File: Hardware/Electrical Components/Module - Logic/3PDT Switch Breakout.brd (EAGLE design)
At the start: 15.2 x 21.3 mm, 2 parts

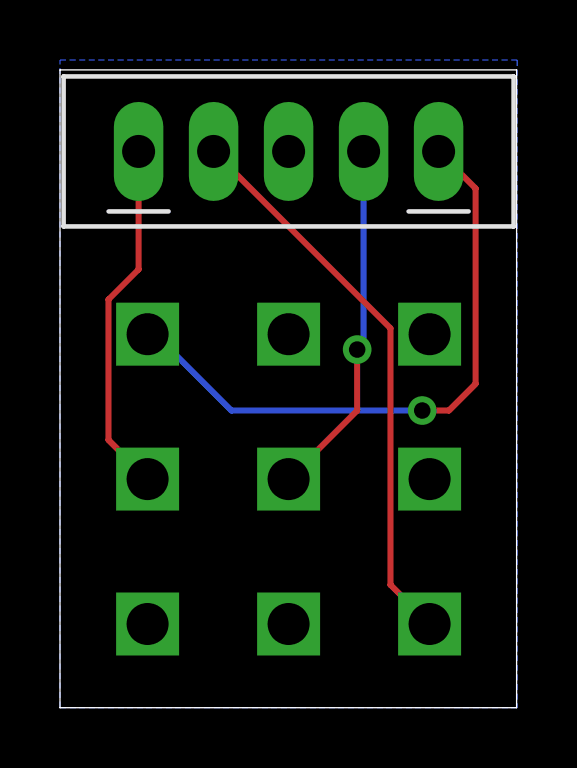
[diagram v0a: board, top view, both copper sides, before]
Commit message: Clarify text in PCBs
O Add text for 3PDT Switch breakout board better PCB annotation
O Rename MOSFET that controls LED for Programming Mode -> P_MOS
+ Add JST Male to BOM Logic Module – Power V8
O Correct excel formula for a total price of Logic Module
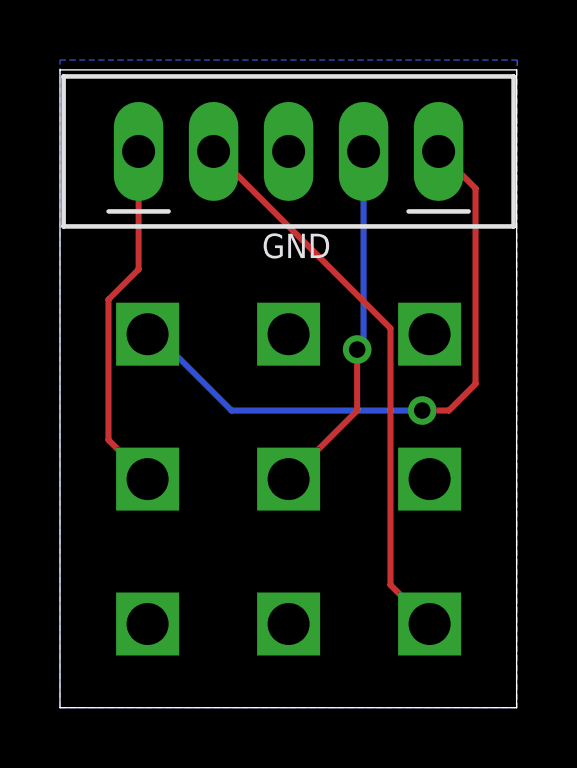
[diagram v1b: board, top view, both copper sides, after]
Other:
- board text added: "Latch"
- board text added: "SD"
- board text added: "Wake_NoSleep"
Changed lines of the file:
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@@
 <wire x1="0" y1="21.26" x2="0" y2="0" width="0" layer="20"/>
 <text x="0.508" y="9.398" size="1" layer="51" rot="R270">ON ON</text>
-<text x="11.938" y="15.113" size="0.6" layer="51">GND</text>
+<text x="6.731" y="14.986" size="0.8128" layer="21">GND</text>
+<text x="5.461" y="16.383" size="0.8128" layer="22" rot="MR270">Latch</text>
+<text x="10.668" y="16.383" size="0.8128" layer="22" rot="MR270">Wake_NoSleep</text>
+<text x="2.921" y="16.383" size="0.8128" layer="22" rot="MR270">SD</text>
+<text x="8.001" y="16.383" size="0.8128" layer="22" rot="MR270">GND</text>
 </plain>
 <attributes>
